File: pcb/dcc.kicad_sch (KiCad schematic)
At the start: 68 parts, among them U10 LM339, U11 LM339, U4 L78L05_SOT89, U5 L79L05_SOT89, U6 LM339, U7 LM339, U8 LM339, U9 4052

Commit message: Add several notes.
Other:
- note added: "0.3 W max"
- note added: "Diodes: max. 1.65 W both. Typically max 0.8 W each (DCC). Resistors: 0.2 W each. Implement cooling!"
- note added: "No pull-up required. Current output."
- note added: "No pull-ups required. Current output."
- note added: "No pull-ups required. Using analog multiplexer."
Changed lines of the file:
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@@
     (effects (font (size 1.27 1.27)) (justify left bottom))
+  )
+  (text "No pull-ups required.\nCurrent output." (at 125.095 29.845 0)
+    (effects (font (size 1.27 1.27)) (justify right bottom))
   )
   (text "J" (at 247.65 21.59 0)
     (effects (font (size 1.27 1.27)) (justify left bottom))
   )
+  (text "Diodes: max. 1.65 W both.\nTypically max 0.8 W each (DCC).\nResistors: 0.2 W each.\nImplement cooling!"
+    (at 164.465 144.145 0)
+    (effects (font (size 1.27 1.27)) (justify left bottom))
+  )
+  (text "No pull-ups required.\nUsing analog multiplexer." (at 211.455 45.085 0)
+    (effects (font (size 1.27 1.27)) (justify right bottom))
+  )
+  (text "0.3 W max" (at 43.815 146.685 0)
+    (effects (font (size 1.27 1.27)) (justify right bottom))
+  )
   (text "J" (at 43.18 21.59 0)
     (effects (font (size 1.27 1.27)) (justify left bottom))
   )
-  (text "-18,5 mV" (at 120.65 125.73 0)
+  (text "No pull-up required.\nCurrent output." (at 147.955 89.535 0)
+    (effects (font (size 1.27 1.27)) (justify right bottom))
+  )
+  (text "-18,5 mV" (at 120.65 126.365 0)
     (effects (font (size 1.27 1.27)) (justify left bottom))
   )
@@
   )
   (symbol (lib_id "4xxx:4052") (at 143.51 43.18 90) (unit 1)
-    (in_bom yes) (on_board yes) (dnp no) (fields_autoplaced)
-    (property "Reference" "U9" (at 120.65 40.9859 0)
-      (effects (font (size 1.27 1.27)) (justify left))
-    )
-    (property "Value" "4052" (at 123.19 40.9859 0)
-      (effects (font (size 1.27 1.27)) (justify left))
+    (in_bom yes) (on_board yes) (dnp no)
+    (property "Reference" "U9" (at 151.13 30.48 90)
+      (effects (font (size 1.27 1.27)))
+    )
+    (property "Value" "4052" (at 151.13 33.02 90)
+      (effects (font (size 1.27 1.27)))
     )
     (property "Footprint" "Package_SO:SO-16_3.9x9.9mm_P1.27mm" (at 143.51 43.18 0)

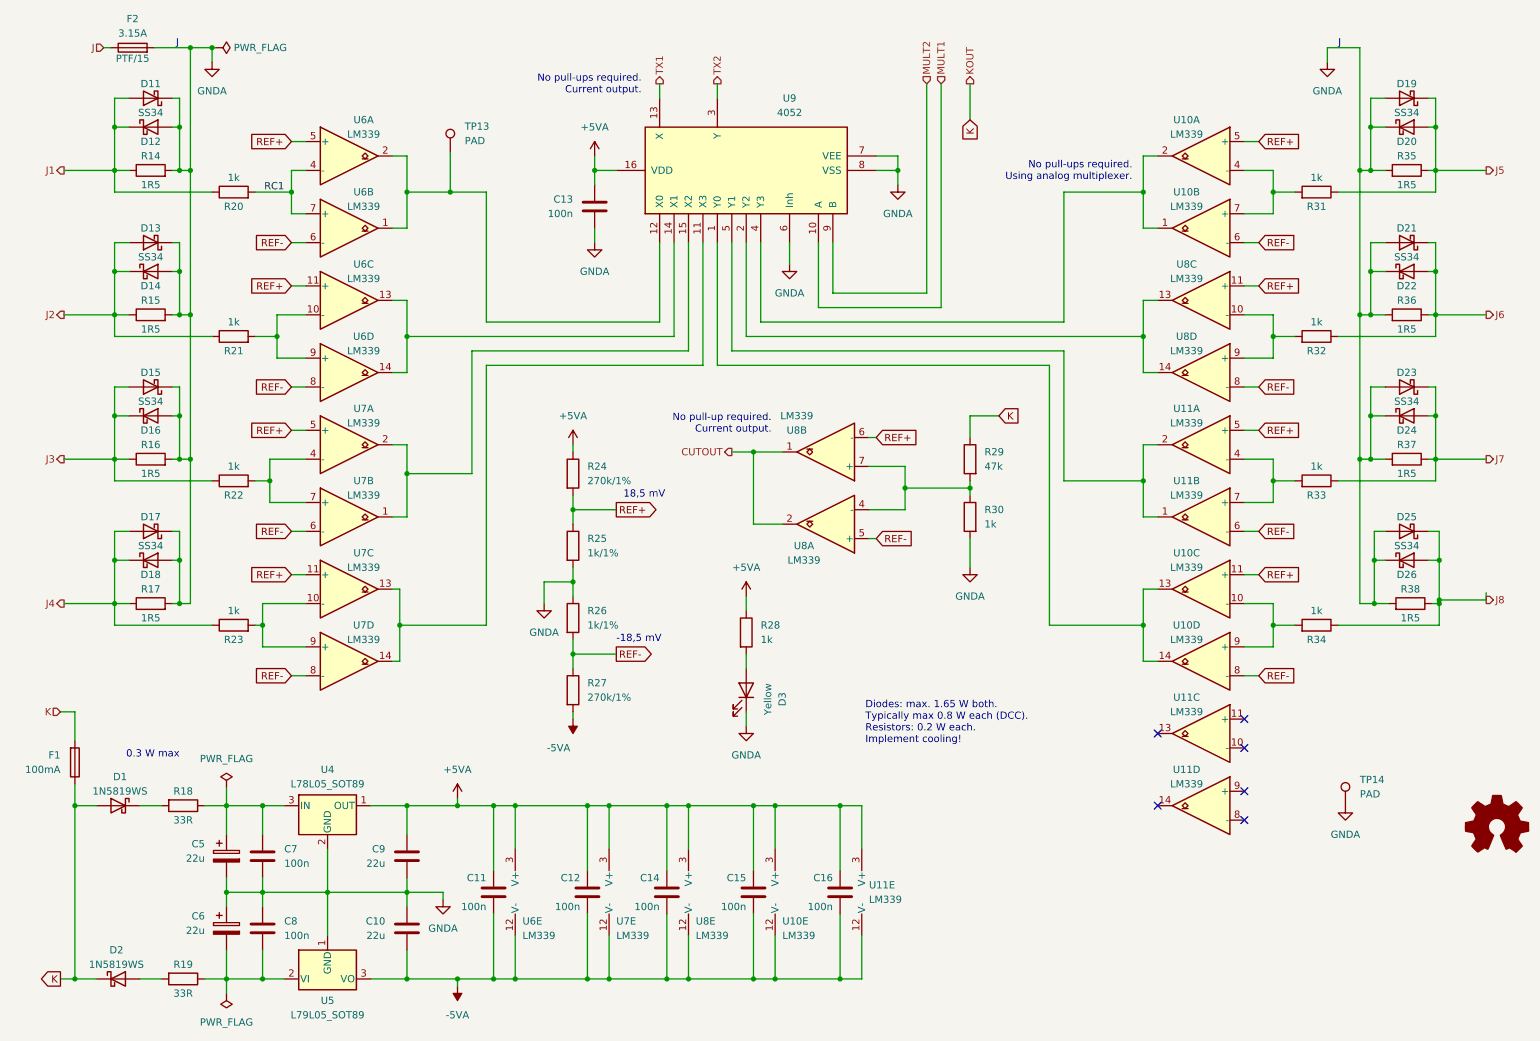
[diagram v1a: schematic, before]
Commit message: Add rest of footprints.
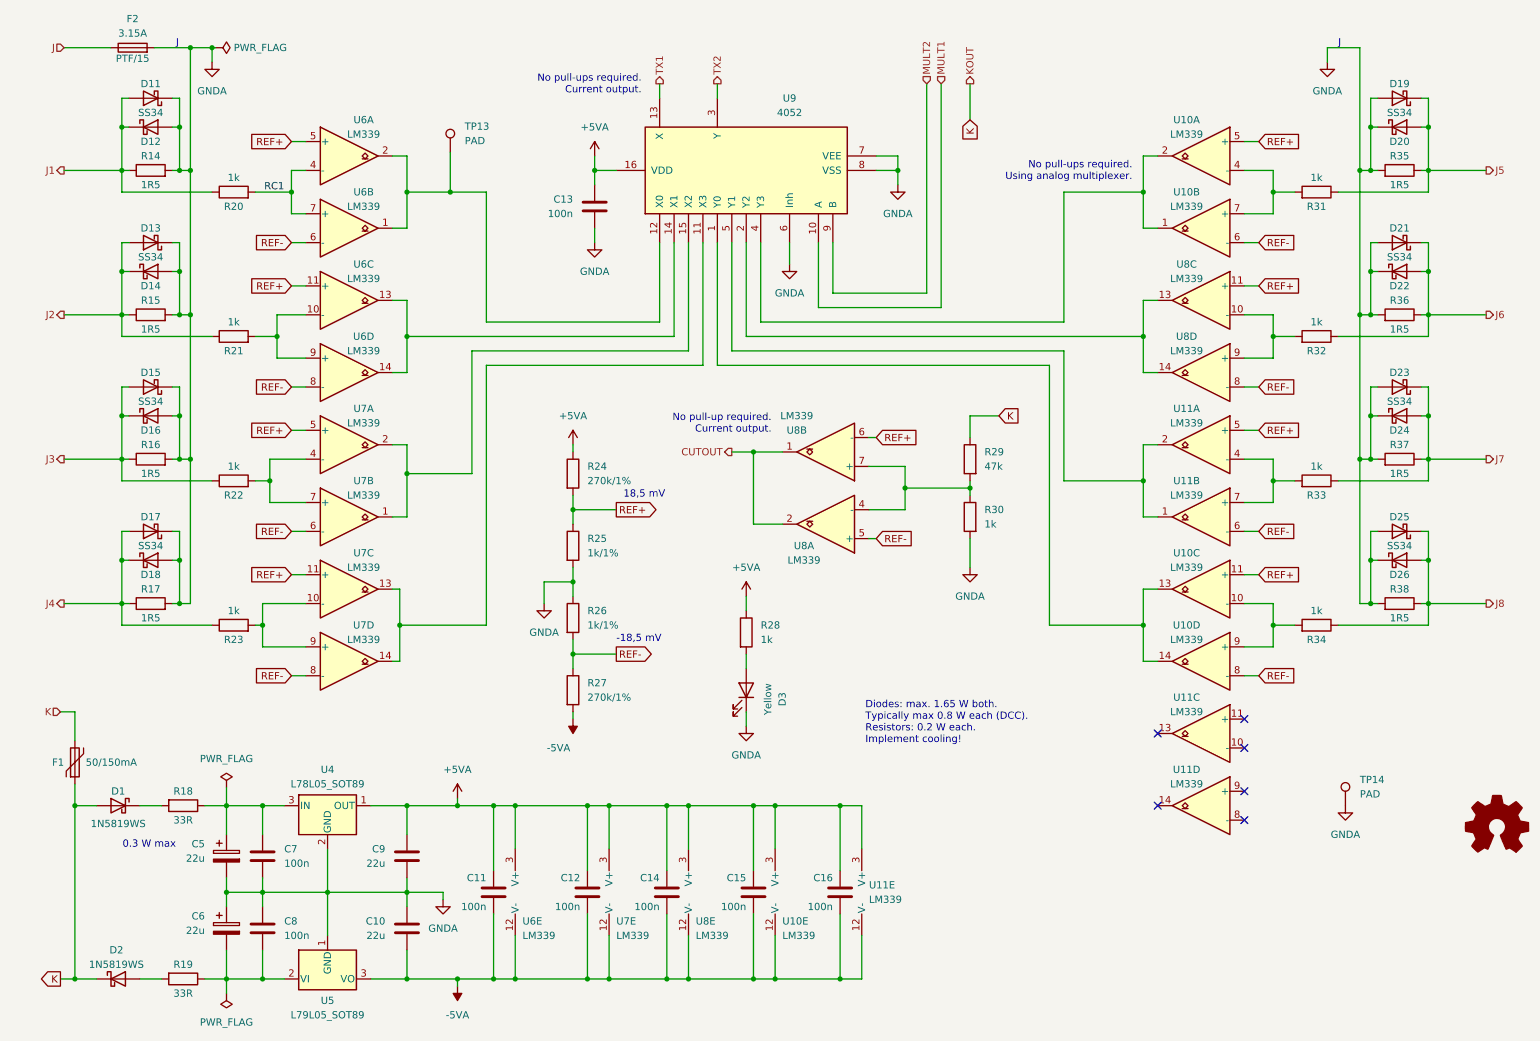
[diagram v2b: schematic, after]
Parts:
- F1: value 100mA -> 50/150mA; footprint (none) -> Fuse:Fuse_1206_3216Metric_Pad1.42x1.75mm_HandSolder; symbol Device:Fuse -> Device:Polyfuse; TME (none) -> 0ZCJ0005FF2E
- R14, R15, R16, R17, R18, R19, R35, R36, R37, R38: footprint (none) -> Resistor_SMD:R_2512_6332Metric
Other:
- moved on the sheet: D19, D20, D21, D22, D23, D24, D25, D26, R35, R36, R37, R38

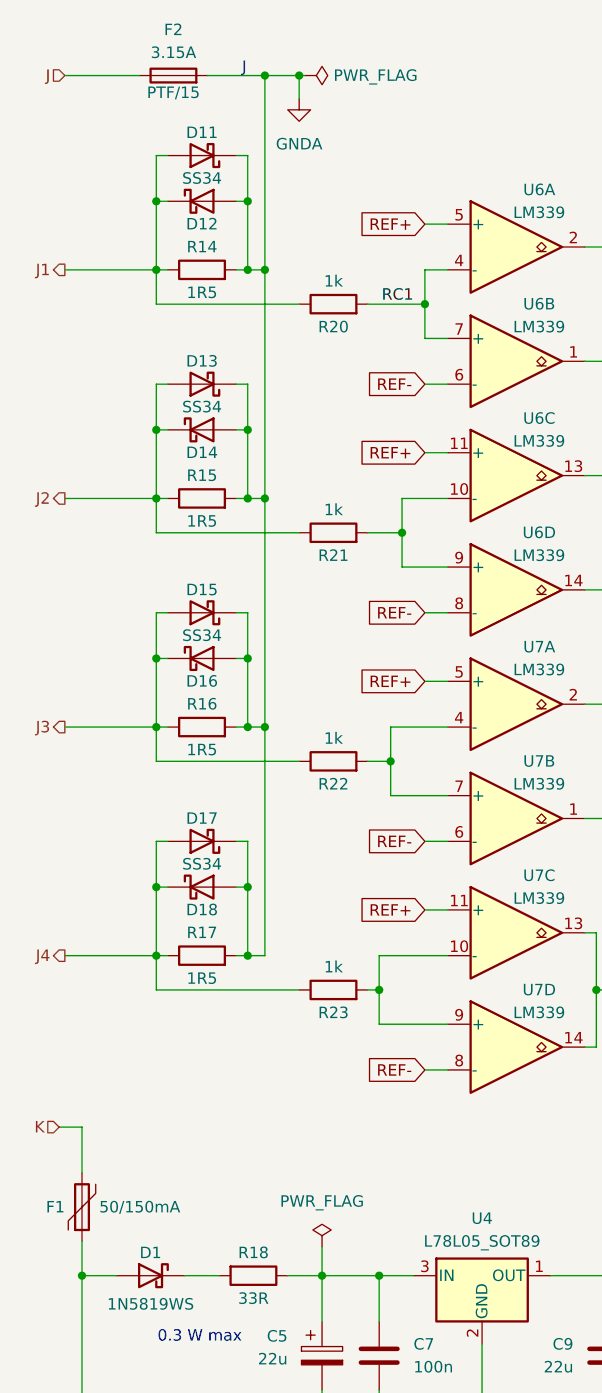
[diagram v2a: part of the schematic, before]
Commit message: Make TME attributes visible.
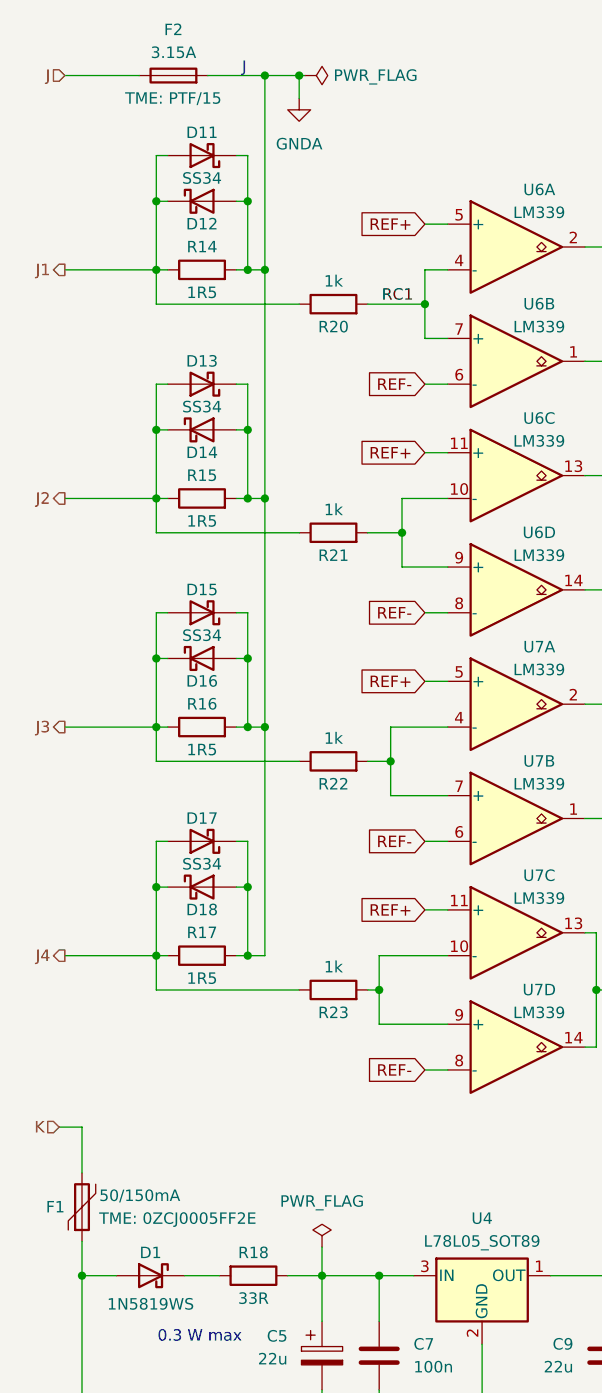
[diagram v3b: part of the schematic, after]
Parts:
- F2: TME (none) -> PTF/15; atribut PTF/15 -> (none)
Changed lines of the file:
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@@
       (effects (font (size 1.27 1.27)) hide)
     )
-    (property "atribut" "PTF/15" (at 35.56 23.495 90)
+    (property "TME" "PTF/15" (at 35.56 24.13 90) (show_name)
       (effects (font (size 1.27 1.27)))
     )
@@
       (effects (font (size 1.27 1.27)) (justify right))
     )
-    (property "Value" "50/150mA" (at 27.305 147.32 0)
+    (property "Value" "50/150mA" (at 27.305 146.05 0)
       (effects (font (size 1.27 1.27)) (justify left))
     )
@@
       (effects (font (size 1.27 1.27)) hide)
     )
-    (property "TME" "0ZCJ0005FF2E" (at 25.4 147.32 0)
-      (effects (font (size 1.27 1.27)) hide)
-    )
-    (pin "1")
+    (property "TME" "0ZCJ0005FF2E" (at 27.305 148.59 0) (show_name)
+      (effects (font (size 1.27 1.27)) (justify left))
+    )
+    (pin "1")

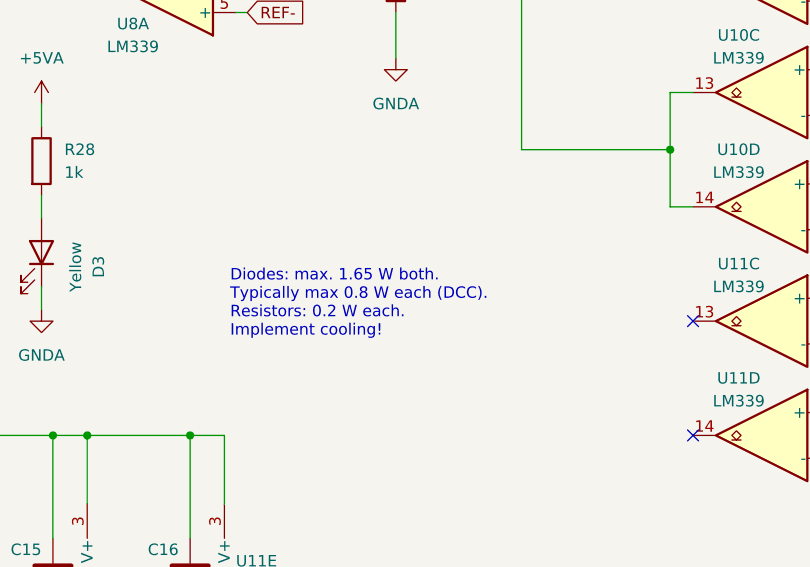
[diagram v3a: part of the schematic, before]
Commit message: Update note regarding diode thermal loss.
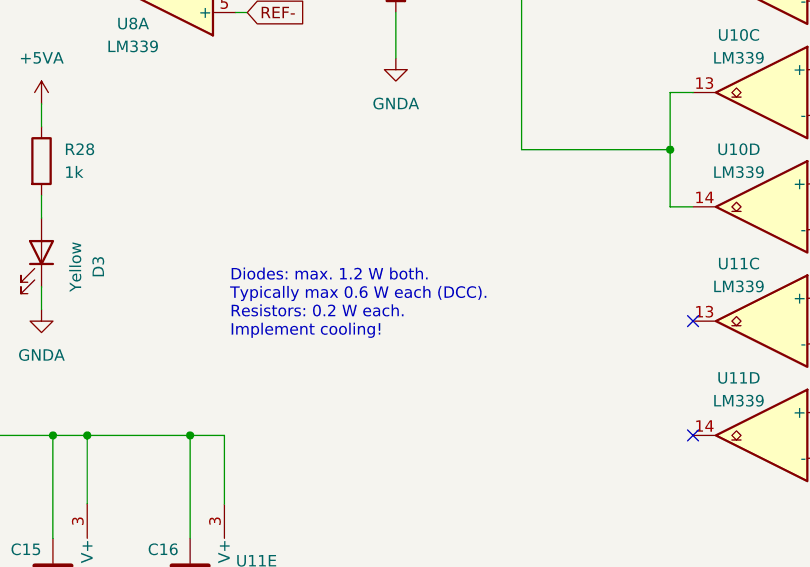
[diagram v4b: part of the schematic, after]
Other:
- note added: "Diodes: max. 1.2 W both. Typically max 0.6 W each (DCC). Resistors: 0.2 W each. Implement cooling!"
- note removed: "Diodes: max. 1.65 W both. Typically max 0.8 W each (DCC). Resistors: 0.2 W each. Implement cooling!"
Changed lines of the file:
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@@
     (effects (font (size 1.27 1.27)) (justify left bottom))
   )
-  (text "Diodes: max. 1.65 W both.\nTypically max 0.8 W each (DCC).\nResistors: 0.2 W each.\nImplement cooling!"
+  (text "Diodes: max. 1.2 W both.\nTypically max 0.6 W each (DCC).\nResistors: 0.2 W each.\nImplement cooling!"
     (at 164.465 144.145 0)
     (effects (font (size 1.27 1.27)) (justify left bottom))

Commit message: PCB WIP.
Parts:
- R14, R15, R16, R17, R35, R36, R37, R38: footprint Resistor_SMD:R_2512_6332Metric -> Resistor_SMD:R_2512_6332Metric_Pad1.40x3.35mm_HandSolder
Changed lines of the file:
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@@
       (effects (font (size 1.27 1.27)))
     )
-    (property "Footprint" "Resistor_SMD:R_2512_6332Metric" (at 258.445 44.958 90)
+    (property "Footprint" "Resistor_SMD:R_2512_6332Metric_Pad1.40x3.35mm_HandSolder" (at 258.445 44.958 90)
       (effects (font (size 1.27 1.27)) hide)
     )
@@
       (effects (font (size 1.27 1.27)))
     )
-    (property "Footprint" "Resistor_SMD:R_2512_6332Metric" (at 258.445 70.358 90)
+    (property "Footprint" "Resistor_SMD:R_2512_6332Metric_Pad1.40x3.35mm_HandSolder" (at 258.445 70.358 90)
       (effects (font (size 1.27 1.27)) hide)
     )
@@
       (effects (font (size 1.27 1.27)))
     )
-    (property "Footprint" "Resistor_SMD:R_2512_6332Metric" (at 258.445 95.758 90)
+    (property "Footprint" "Resistor_SMD:R_2512_6332Metric_Pad1.40x3.35mm_HandSolder" (at 258.445 95.758 90)
       (effects (font (size 1.27 1.27)) hide)
     )
@@
       (effects (font (size 1.27 1.27)))
     )
-    (property "Footprint" "Resistor_SMD:R_2512_6332Metric" (at 258.445 121.158 90)
+    (property "Footprint" "Resistor_SMD:R_2512_6332Metric_Pad1.40x3.35mm_HandSolder" (at 258.445 121.158 90)
       (effects (font (size 1.27 1.27)) hide)
     )
@@
       (effects (font (size 1.27 1.27)))
     )
-    (property "Footprint" "Resistor_SMD:R_2512_6332Metric" (at 38.735 95.758 90)
+    (property "Footprint" "Resistor_SMD:R_2512_6332Metric_Pad1.40x3.35mm_HandSolder" (at 38.735 95.758 90)
       (effects (font (size 1.27 1.27)) hide)
     )
@@
       (effects (font (size 1.27 1.27)))
     )
-    (property "Footprint" "Resistor_SMD:R_2512_6332Metric" (at 38.735 121.158 90)
+    (property "Footprint" "Resistor_SMD:R_2512_6332Metric_Pad1.40x3.35mm_HandSolder" (at 38.735 121.158 90)
       (effects (font (size 1.27 1.27)) hide)
     )
@@
       (effects (font (size 1.27 1.27)))
     )
-    (property "Footprint" "Resistor_SMD:R_2512_6332Metric" (at 38.735 70.358 90)
+    (property "Footprint" "Resistor_SMD:R_2512_6332Metric_Pad1.40x3.35mm_HandSolder" (at 38.735 70.358 90)
       (effects (font (size 1.27 1.27)) hide)
     )
@@
       (effects (font (size 1.27 1.27)))
     )
-    (property "Footprint" "Resistor_SMD:R_2512_6332Metric" (at 38.735 44.958 90)
-      (effects (font (size 1.27 1.27)) hide)
-    )
+    (property "Footprint" "Resistor_SMD:R_2512_6332Metric_Pad1.40x3.35mm_HandSolder" (at 38.735 44.958 90)
+      (effects (font (size 1.27 1.27)) hide)
+    )
